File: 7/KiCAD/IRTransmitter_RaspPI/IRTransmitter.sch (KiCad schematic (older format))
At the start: 12 parts, among them J1 Conn_02x08_Odd_Even, Q1 BC33740TA, Q2 BC33740TA

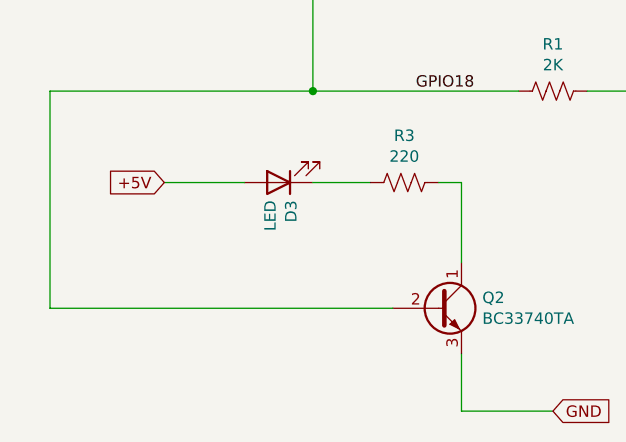
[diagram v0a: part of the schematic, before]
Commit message: Corrected RaspPI IR emitter.
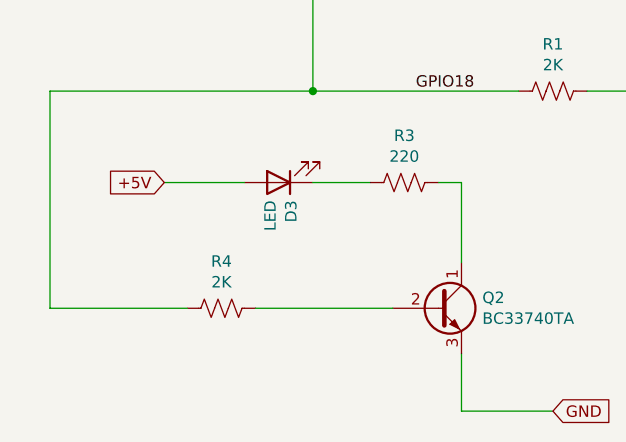
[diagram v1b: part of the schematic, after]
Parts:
- added R4: 2K, Resistor_THT:R_Axial_DIN0207_L6.3mm_D2.5mm_P10.16mm_Horizontal, symbol Device:R_US
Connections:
- net GPIO18: now also R4.2; no longer Q2.2 (B)
- new net: Q2.2 (B), R4.1
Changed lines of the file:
@@
 Wire Wire Line
 	850  3300 850  4250
-Wire Wire Line
-	850  4250 2350 4250
 Connection ~ 2000 3300
 Wire Wire Line
@@
 Text GLabel 3050 4700 2    50   Input ~ 0
 GND
+$Comp
+L Device:R_US R4
+U 1 1 61A56F24
+P 1600 4250
+F 0 "R4" V 1395 4250 50  0000 C CNN
+F 1 "2K" V 1486 4250 50  0000 C CNN
+F 2 "Resistor_THT:R_Axial_DIN0207_L6.3mm_D2.5mm_P10.16mm_Horizontal" V 1640 4240 50  0001 C CNN
+F 3 "~" H 1600 4250 50  0001 C CNN
+	1    1600 4250
+	0    1    1    0
+$EndComp
+Wire Wire Line
+	1750 4250 2350 4250
+Wire Wire Line
+	1450 4250 850  4250
 $EndSCHEMATC

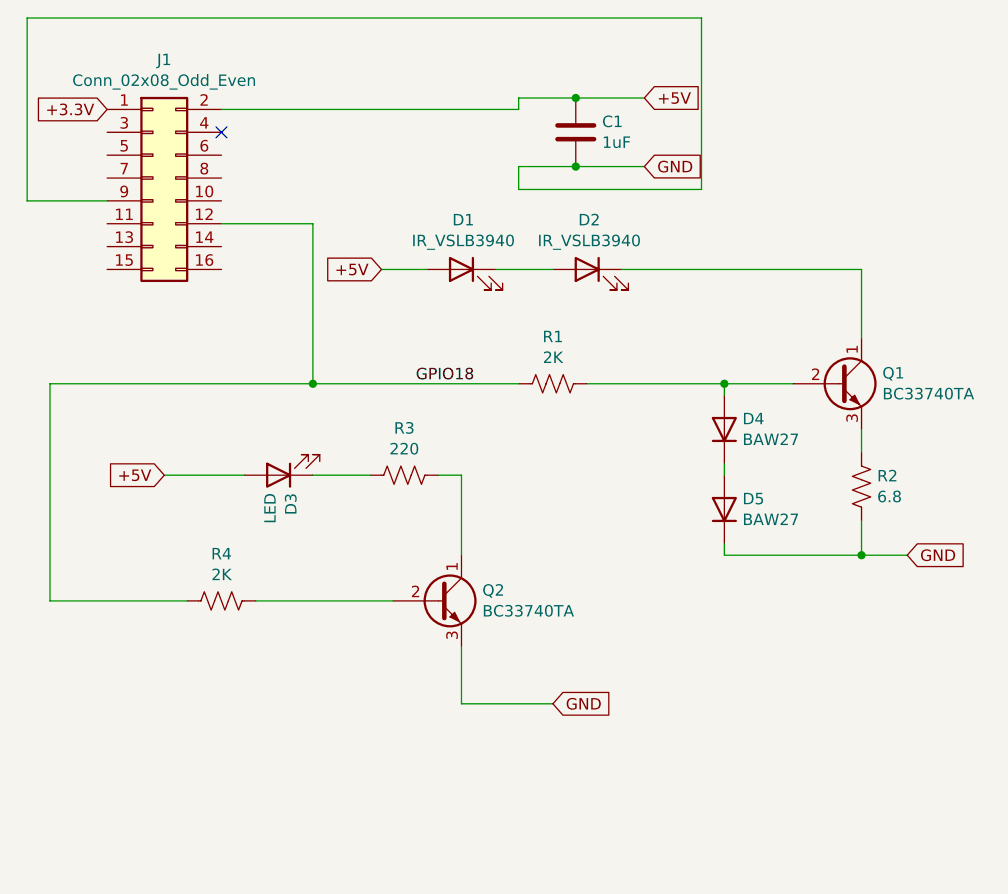
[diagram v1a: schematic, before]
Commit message: Corrected RaspPI IR emitter.
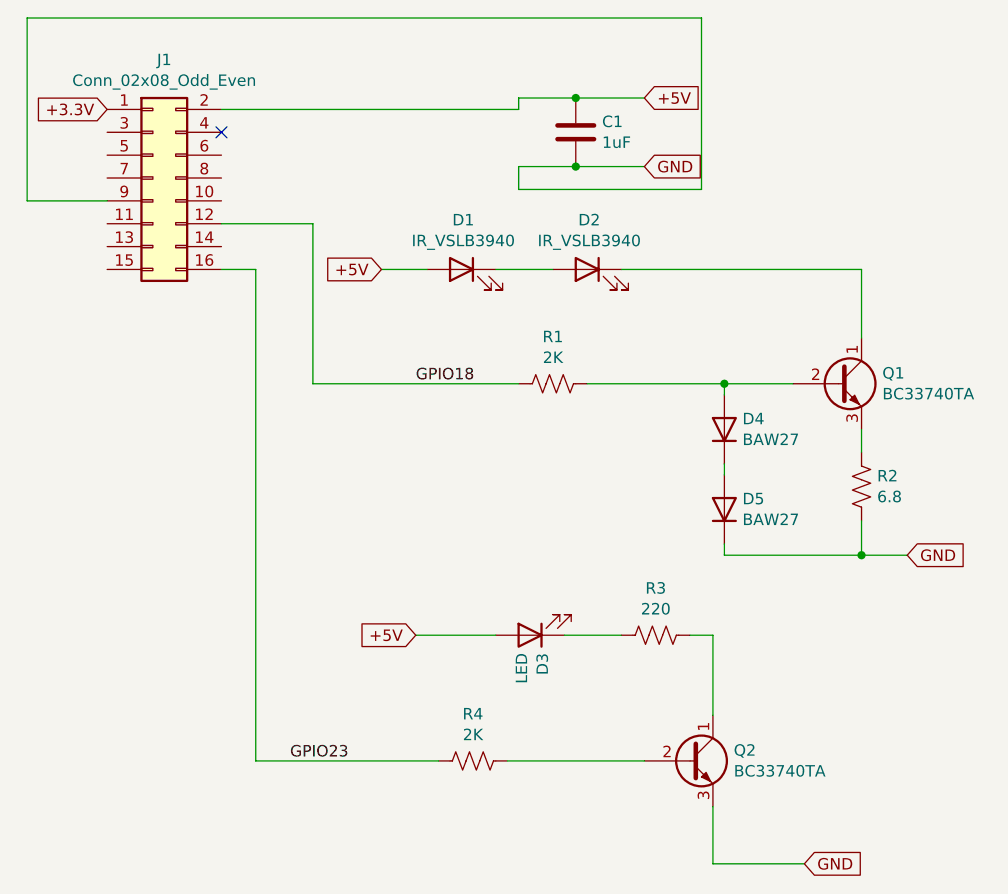
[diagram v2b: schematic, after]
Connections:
- net GPIO18: no longer R4.2
- net GPIO23: now reaches J1.16 (Pin_16)
- net GPIO23: now also R4.2
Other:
- moved on the sheet: D3, Q2, R3, R4
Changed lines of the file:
@@
 L Device:LED D3
 U 1 1 5D23ECDE
-P 1850 3700
-F 0 "D3" V 1795 3778 50  0000 L CNN
-F 1 "LED" V 1886 3778 50  0000 L CNN
-F 2 "LED_THT:LED_D5.0mm" H 1850 3700 50  0001 C CNN
-F 3 "~" H 1850 3700 50  0001 C CNN
-	1    1850 3700
+P 2950 4400
+F 0 "D3" V 2895 4478 50  0000 L CNN
+F 1 "LED" V 2986 4478 50  0000 L CNN
+F 2 "LED_THT:LED_D5.0mm" H 2950 4400 50  0001 C CNN
+F 3 "~" H 2950 4400 50  0001 C CNN
+	1    2950 4400
 	-1   0    0    1
 $EndComp
@@
 L Device:R_US R3
 U 1 1 5D23F264
-P 2400 3700
-F 0 "R3" V 2195 3700 50  0000 C CNN
-F 1 "220" V 2286 3700 50  0000 C CNN
-F 2 "Resistor_THT:R_Axial_DIN0207_L6.3mm_D2.5mm_P10.16mm_Horizontal" V 2440 3690 50  0001 C CNN
-F 3 "~" H 2400 3700 50  0001 C CNN
-	1    2400 3700
+P 3500 4400
+F 0 "R3" V 3295 4400 50  0000 C CNN
+F 1 "220" V 3386 4400 50  0000 C CNN
+F 2 "Resistor_THT:R_Axial_DIN0207_L6.3mm_D2.5mm_P10.16mm_Horizontal" V 3540 4390 50  0001 C CNN
+F 3 "~" H 3500 4400 50  0001 C CNN
+	1    3500 4400
 	0    1    1    0
 $EndComp
@@
 L Transistor_BJT:BC337 Q2
 U 1 1 61A12D52
-P 2550 4250
-F 0 "Q2" H 2741 4296 50  0000 L CNN
-F 1 "BC33740TA" H 2741 4205 50  0000 L CNN
-F 2 "Transistors:NPN_Transistor" H 2750 4175 50  0001 L CIN
-F 3 "http://www.nxp.com/documents/data_sheet/BC817_BC817W_BC337.pdf" H 2550 4250 50  0001 L CNN
-	1    2550 4250
+P 3650 4950
+F 0 "Q2" H 3841 4996 50  0000 L CNN
+F 1 "BC33740TA" H 3841 4905 50  0000 L CNN
+F 2 "Transistors:NPN_Transistor" H 3850 4875 50  0001 L CIN
+F 3 "http://www.nxp.com/documents/data_sheet/BC817_BC817W_BC337.pdf" H 3650 4950 50  0001 L CNN
+	1    3650 4950
 	1    0    0    -1
 $EndComp
-Text GLabel 1350 3700 0    50   Input ~ 0
+Text GLabel 2450 4400 0    50   Input ~ 0
 +5V
 Wire Wire Line
-	1350 3700 1700 3700
+	2450 4400 2800 4400
 Wire Wire Line
-	2000 3700 2250 3700
+	3100 4400 3350 4400
 Wire Wire Line
-	2550 3700 2650 3700
+	3650 4400 3750 4400
 Wire Wire Line
-	2650 3700 2650 4050
+	3750 4400 3750 4750
 Wire Wire Line
-	2000 3300 850  3300
+	3750 5150 3750 5400
 Wire Wire Line
-	850  3300 850  4250
-Connection ~ 2000 3300
-Wire Wire Line
-	2650 4450 2650 4700
-Wire Wire Line
-	2650 4700 3050 4700
-Text GLabel 3050 4700 2    50   Input ~ 0
+	3750 5400 4150 5400
+Text GLabel 4150 5400 2    50   Input ~ 0
 GND
 $Comp
 L Device:R_US R4
 U 1 1 61A56F24
-P 1600 4250
-F 0 "R4" V 1395 4250 50  0000 C CNN
-F 1 "2K" V 1486 4250 50  0000 C CNN
-F 2 "Resistor_THT:R_Axial_DIN0207_L6.3mm_D2.5mm_P10.16mm_Horizontal" V 1640 4240 50  0001 C CNN
-F 3 "~" H 1600 4250 50  0001 C CNN
-	1    1600 4250
+P 2700 4950
+F 0 "R4" V 2495 4950 50  0000 C CNN
+F 1 "2K" V 2586 4950 50  0000 C CNN
+F 2 "Resistor_THT:R_Axial_DIN0207_L6.3mm_D2.5mm_P10.16mm_Horizontal" V 2740 4940 50  0001 C CNN
+F 3 "~" H 2700 4950 50  0001 C CNN
+	1    2700 4950
 	0    1    1    0
 $EndComp
 Wire Wire Line
-	1750 4250 2350 4250
+	2850 4950 3450 4950
 Wire Wire Line
-	1450 4250 850  4250
+	2550 4950 1750 4950
+Wire Wire Line
+	1600 2800 1750 2800
+Wire Wire Line
+	1750 2800 1750 4950
+Text Label 1900 4950 0    50   ~ 0
+GPIO23
 $EndSCHEMATC

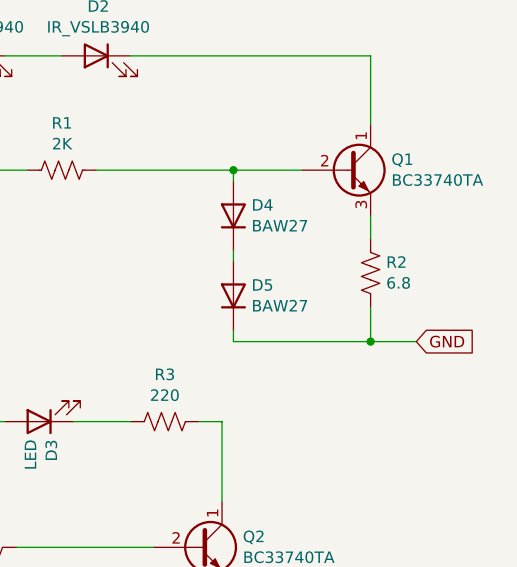
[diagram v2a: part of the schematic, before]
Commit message: Updated schematic/PCB of RaspPI IR Emitter.
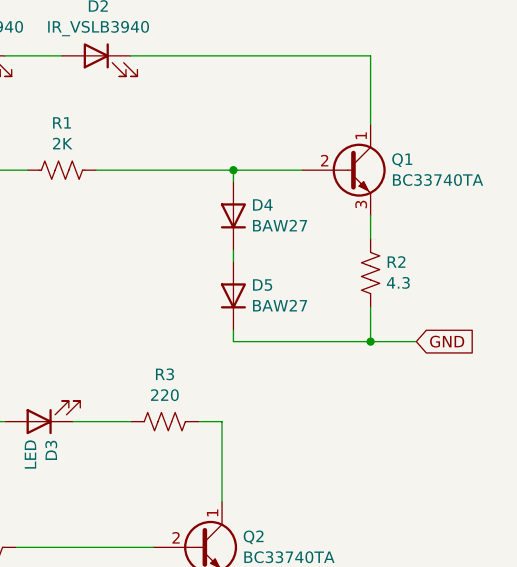
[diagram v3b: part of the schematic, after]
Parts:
- R2: value 6.8 -> 4.3
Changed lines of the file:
@@
 P 4400 3750
 F 0 "R2" H 4468 3796 50  0000 L CNN
-F 1 "6.8" H 4468 3705 50  0000 L CNN
+F 1 "4.3" H 4468 3705 50  0000 L CNN
 F 2 "Resistor_THT:R_Axial_DIN0207_L6.3mm_D2.5mm_P10.16mm_Horizontal" V 4440 3740 50  0001 C CNN
 F 3 "~" H 4400 3750 50  0001 C CNN
